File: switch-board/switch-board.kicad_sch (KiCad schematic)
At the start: 16 parts

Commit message: finalized rev A PCB
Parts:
- removed J?: 12V_IN, symbol Connector:Conn_01x01_Female
- removed J?: RF_NO, symbol Connector:Conn_01x01_Female
- removed J?: RF_IN, symbol Connector:Conn_01x01_Female
- removed J?: CTRL, symbol Connector:Conn_01x02_Female
- removed J?: RF_NC, symbol Connector:Conn_01x01_Female
- added C1: 1uF, Capacitor_SMD:C_0805_2012Metric_Pad1.18x1.45mm_HandSolder, symbol Device:C_Small
- added H1, H2: MountingHole_Pad, MountingHole:MountingHole_4.3mm_M4_Pad, symbol Mechanical:MountingHole_Pad
- added J1: VIN, TestPoint:TestPoint_Pad_1.5x1.5mm, symbol Connector:Conn_01x01_Female
- added J2: CTRL, TestPoint:TestPoint_Pad_1.5x1.5mm, symbol Connector:Conn_01x01_Female
- added J3: RF_XOUT, conn:Coax_Edge_2.54_1.27, symbol Connector:Conn_Coaxial
- added J4: RF_XIN, conn:Coax_Edge_2.54_1.27, symbol Connector:Conn_Coaxial
- added J5: RF_YIN, conn:Coax_Edge_2.54_1.27, symbol Connector:Conn_Coaxial
- added J6: RF_YOUT, conn:Coax_Edge_2.54_1.27, symbol Connector:Conn_Coaxial
- added J7: GND, TestPoint:TestPoint_Pad_1.5x1.5mm, symbol Connector:Conn_01x01_Female
- C2: renamed from C?; footprint (none) -> Capacitor_SMD:C_0805_2012Metric_Pad1.18x1.45mm_HandSolder
- C3, C4, C5: renamed from C?; footprint (none) -> Capacitor_SMD:C_1812_4532Metric_Pad1.57x3.40mm_HandSolder
- D1: renamed from D?; value LED_RGBA -> EAST1616RGBB2; footprint (none) -> led:LED_SMD_1616_RGBA
- D2: renamed from D?; value 1N418 -> 1N4148; footprint (none) -> Diode_SMD:D_SOD-323_HandSoldering
- R1, R2, R3: renamed from R?; footprint (none) -> Resistor_SMD:R_0805_2012Metric_Pad1.20x1.40mm_HandSolder
- gave numbers to parts that had none: 2
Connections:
- net GND: now also C1.1, H1.1, H2.1, J3.2 (Ext), J4.2 (Ext), J5.2 (Ext), J6.2 (Ext), J7.1 (Pin_1)
- net at C5.2, K1.4: now also J5.1 (In), J6.1 (In)
- net at D1.4 (A), D2.1 (K), K1.5: now also C1.2, J1.1 (Pin_1)
- net at C3.2, K1.2: now also J3.1 (In)
- net at C4.2, K1.3: now also J4.1 (In)
- net at R2.1: now also J2.1 (Pin_1)
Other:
- moved on the sheet: C2, C3, C4, C5, D1, D2, K1, Q1, R1, R2, R3

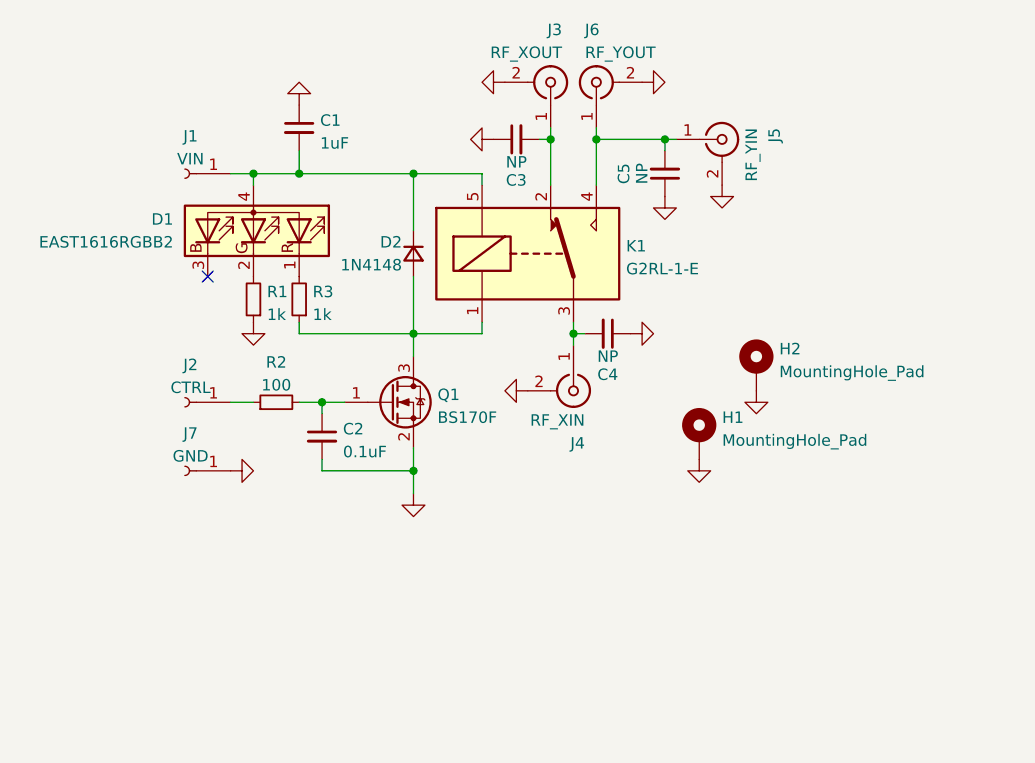
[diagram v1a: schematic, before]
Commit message: finalized single-point switch design, more work on 4x4 matrix
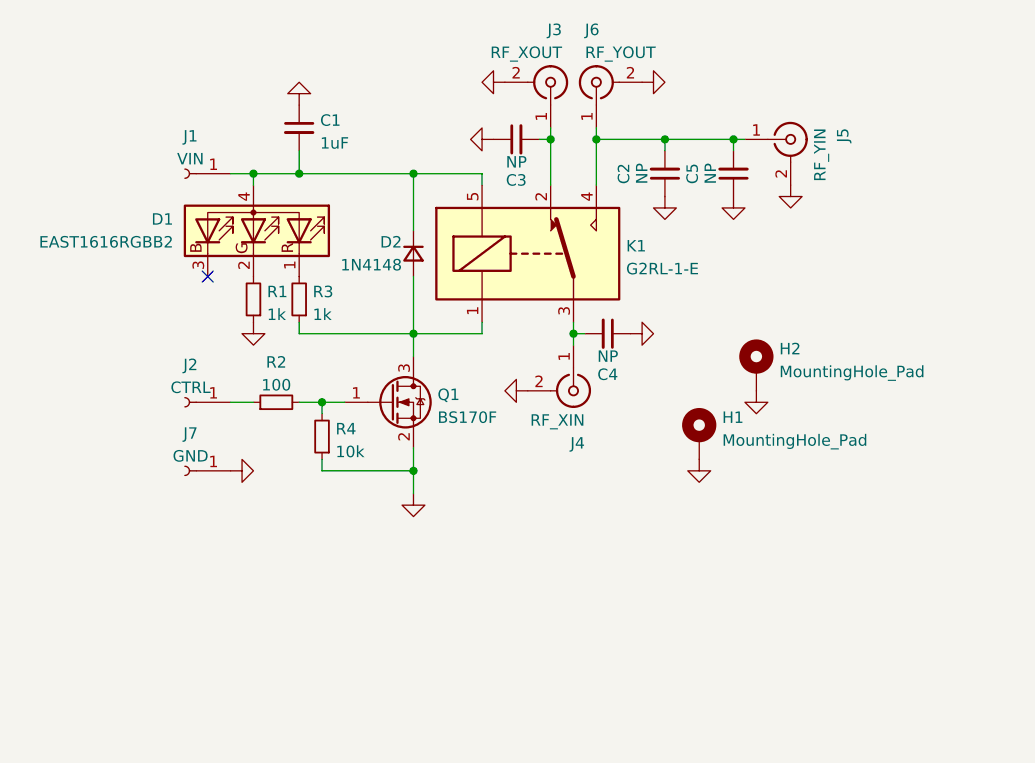
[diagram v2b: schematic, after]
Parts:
- added R4: 10k, Resistor_SMD:R_0805_2012Metric_Pad1.20x1.40mm_HandSolder, symbol Device:R_Small
- C2: value 0.1uF -> NP; footprint Capacitor_SMD:C_0805_2012Metric_Pad1.18x1.45mm_HandSolder -> Capacitor_SMD:C_1812_4532Metric_Pad1.57x3.40mm_HandSolder
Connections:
- net GND: now also C2.1, R4.1; no longer C2.2
- net at C5.2, J5.1 (In), J6.1 (In)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: now also C2.2
- net at Q1.1 (G), R2.2: now also R4.2; no longer C2.1
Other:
- company: (none) -> W3AXL
- title: (none) -> Single Crossbar Switch Point
- moved on the sheet: C5, J5
